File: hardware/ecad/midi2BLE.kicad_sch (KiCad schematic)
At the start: 0 parts

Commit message: Finsihed power schematic, but needs work... pcb has lots of errors still
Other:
- added sheet Battery Sense (battery_sense.kicad_sch)
- added sheet ESP32_S3 (esp32.kicad_sch)
- added sheet OLED UI (oled_ui.kicad_sch)
- added sheet Power (power.kicad_sch)
- added sheet USB Data (usb_data.kicad_sch)
- added sheet VBUS Switching (vbus_switching.kicad_sch)
- note added: "ADC battery monitor"
- note added: "BLE + UI + control"
- note added: "Battery/charging/regulators"
- note added: "Display + status"
- note added: "Keyboard 5V source selection"
- note added: "USB mux/port routing"
- company: (none) -> avega systems
- title: (none) -> midi2BLE_Top_Level

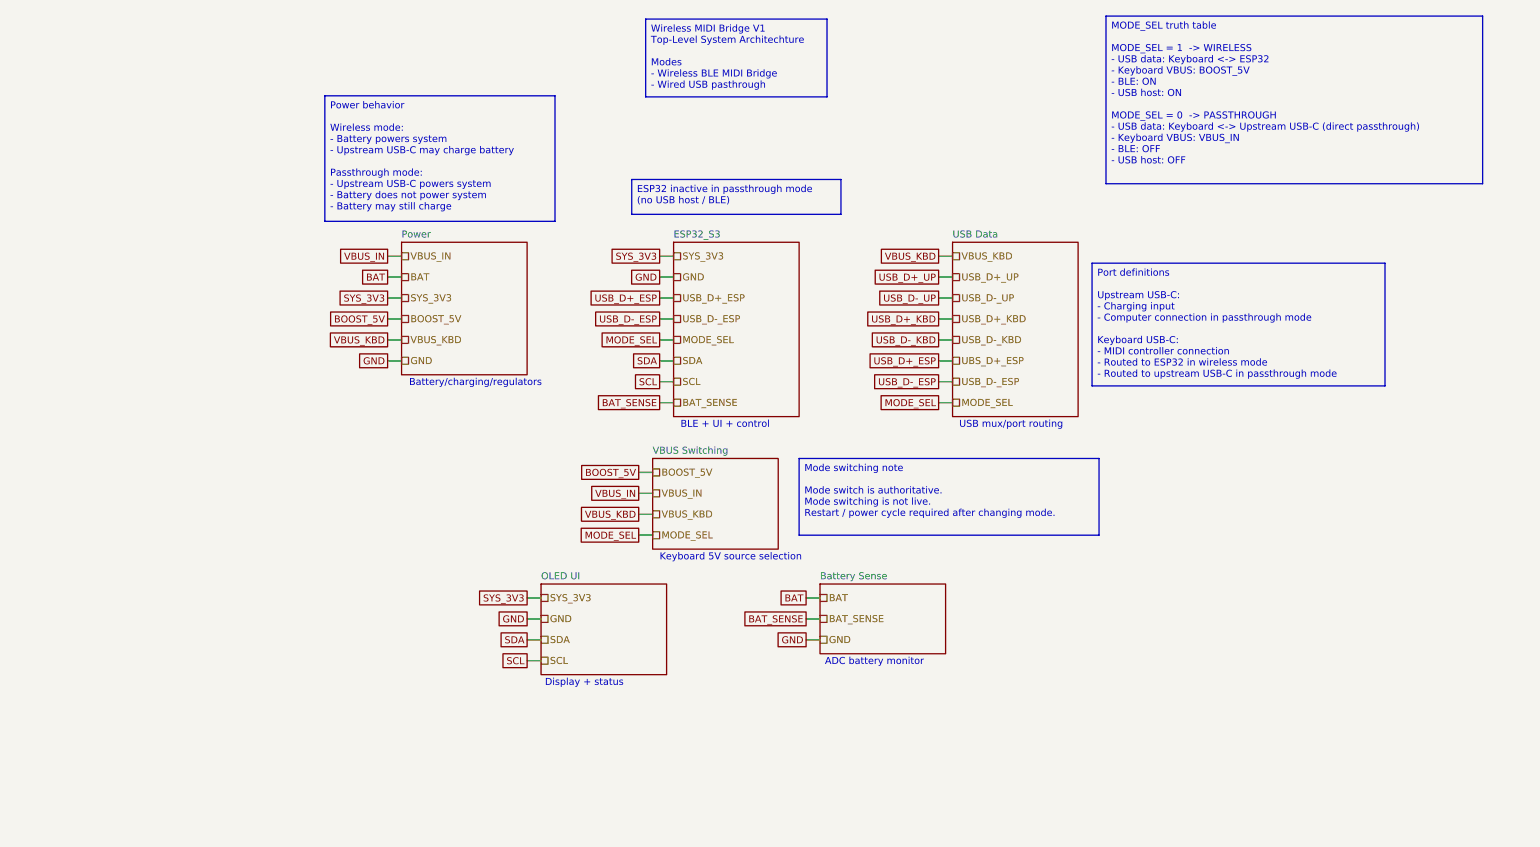
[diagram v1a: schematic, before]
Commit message: Power schematic finished, top level schematic editied to swap from I2c to SPI instead
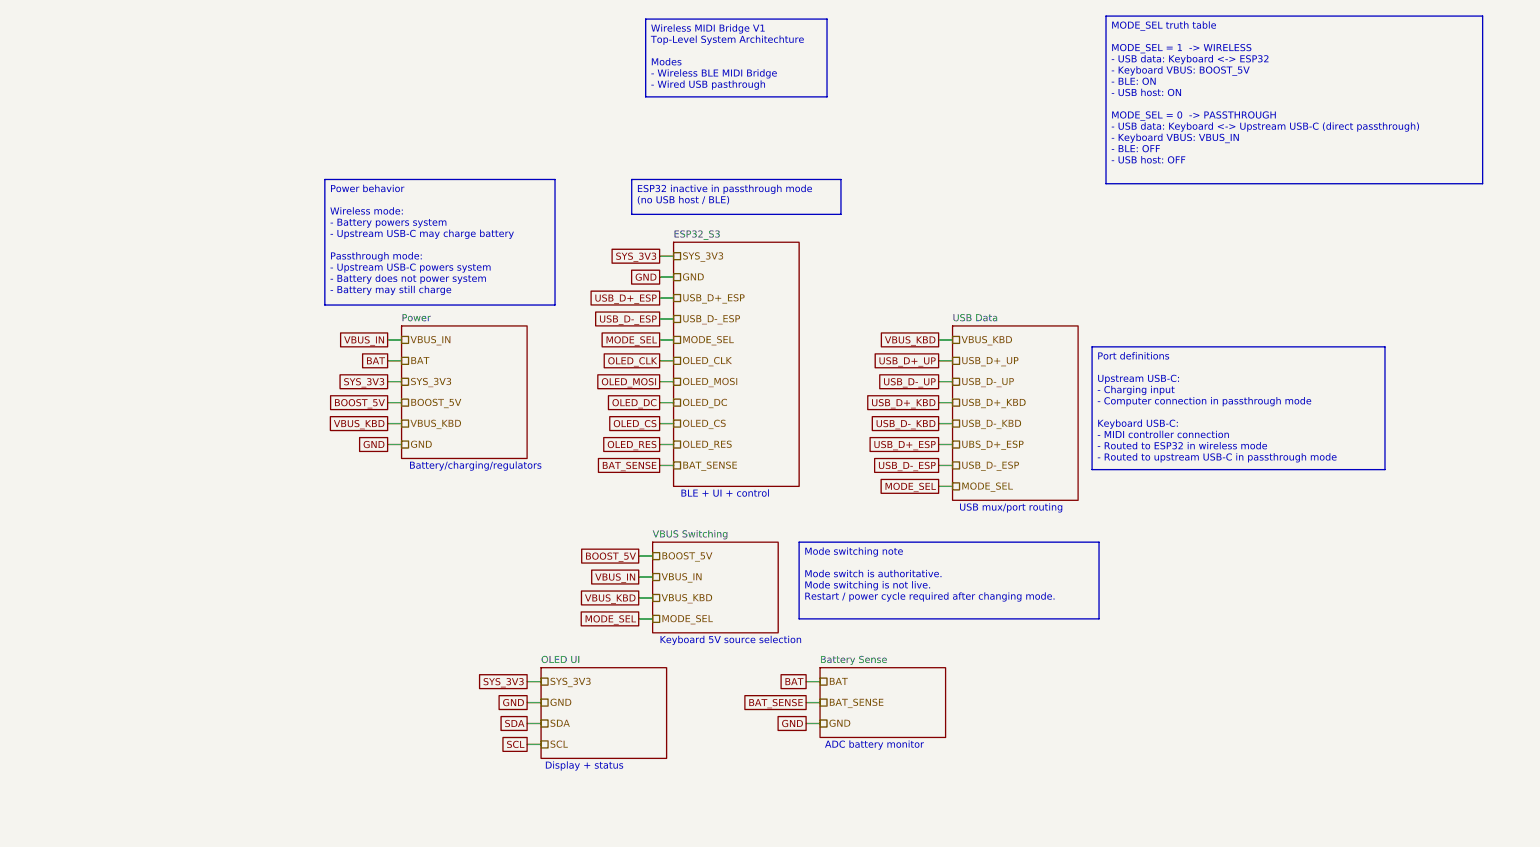
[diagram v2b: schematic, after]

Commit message: finsihed 6/7 sheets, usb_data needs work. Some warnings to be dealt with aswell but no hard errors.
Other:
- sheet Battery Sense ports: added BAT, BAT_SENSE, GND; removed none
- sheet ESP32_S3 ports: added BAT_SENSE, GND, MODE_SEL, OLED_CLK, OLED_CS, OLED_DC, OLED_MOSI, OLED_RES, SYS_3V3, USB_D+_ESP, USB_D-_ESP; removed none
- sheet OLED UI ports: added GND, OLED_CLK, OLED_CS, OLED_DC, OLED_MOSI, OLED_RES, SYS_3V3; removed none
- sheet Power ports: added BAT, BOOST_5V, GND, SYS_3V3, VBUS_IN, VBUS_KBD; removed none
- sheet USB Data ports: added GND, MODE_SEL, SYS_3V3, USB_D+_ESP, USB_D+_KBD, USB_D+_UP, USB_D-_ESP, USB_D-_KBD, USB_D-_UP, VBUS_KBD; removed none
- sheet VBUS Switching ports: added BOOST_5V, GND, MODE_SEL, VBUS_IN, VBUS_KBD; removed none
- company: avega systems -> āvega systems

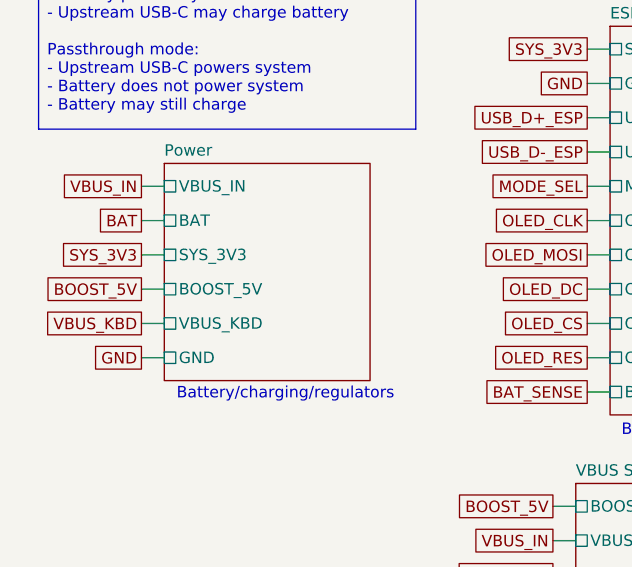
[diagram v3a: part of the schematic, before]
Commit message: Updated schematics to get rid of errors and warnings
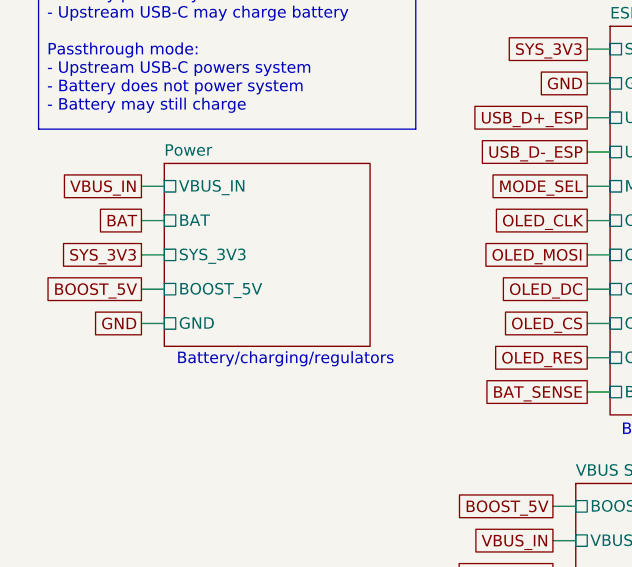
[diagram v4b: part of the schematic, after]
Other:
- sheet Power ports: added none; removed VBUS_KBD
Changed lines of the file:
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@@
 	(text "Battery/charging/regulators"
 		(exclude_from_sim no)
-		(at 98.552 96.774 0)
+		(at 98.552 92.964 0)
 		(effects
 			(font
@@
 	(wire
 		(pts
+			(xy 82.55 88.9) (xy 85.09 88.9)
+		)
+		(stroke
+			(width 0)
+			(type default)
+		)
+	)
+	(wire
+		(pts
 			(xy 132.08 81.28) (xy 134.62 81.28)
 		)
@@
 	(wire
 		(pts
-			(xy 82.55 92.71) (xy 85.09 92.71)
-		)
-		(stroke
-			(width 0)
-			(type default)
-		)
-	)
-	(wire
-		(pts
 			(xy 182.88 92.71) (xy 185.42 92.71)
 		)
@@
 		)
 	)
-	(wire
-		(pts
-			(xy 82.55 88.9) (xy 85.09 88.9)
-		)
-		(stroke
-			(width 0)
-			(type default)
-		)
-	)
 	(global_label "GND"
 		(shape passive)
-		(at 82.55 92.71 180)
-		(fields_autoplaced yes)
-		(effects
-			(font
-				(size 1.27 1.27)
-			)
-			(justify right)
-		)
-		(property "Intersheetrefs" "${INTERSHEET_REFS}"
-			(at 76.8056 92.71 0)
+		(at 82.55 88.9 180)
+		(fields_autoplaced yes)
+		(effects
+			(font
+				(size 1.27 1.27)
+			)
+			(justify right)
+		)
+		(property "Intersheetrefs" "${INTERSHEET_REFS}"
+			(at 76.8056 88.9 0)
 			(hide yes)
 			(show_name no)
@@
 		(property "Intersheetrefs" "${INTERSHEET_REFS}"
 			(at 118.5946 113.03 0)
-			(hide yes)
-			(show_name no)
-			(do_not_autoplace no)
-			(effects
-				(font
-					(size 1.27 1.27)
-				)
-				(justify right)
-			)
-		)
-	)
-	(global_label "VBUS_KBD"
-		(shape passive)
-		(at 82.55 88.9 180)
-		(fields_autoplaced yes)
-		(effects
-			(font
-				(size 1.27 1.27)
-			)
-			(justify right)
-		)
-		(property "Intersheetrefs" "${INTERSHEET_REFS}"
-			(at 70.9999 88.9 0)
 			(hide yes)
 			(show_name no)
@@
 	(sheet
 		(at 85.09 71.12)
-		(size 22.86 24.13)
+		(size 22.86 20.32)
 		(exclude_from_sim no)
 		(in_bom yes)
@@
 		)
 		(property "Sheetfile" "power.kicad_sch"
-			(at 85.09 95.8346 0)
+			(at 85.09 92.0246 0)
 			(hide yes)
 			(show_name no)
@@
 		)
 		(pin "GND" passive
-			(at 85.09 92.71 180)
+			(at 85.09 88.9 180)
 			(effects
 				(font
@@
 			(effects
 				(font
-					(size 1.27 1.27)
-				)
-				(justify left)
-			)
-		)
-		(pin "VBUS_KBD" passive
-			(at 85.09 88.9 180)
-			(effects
-				(font

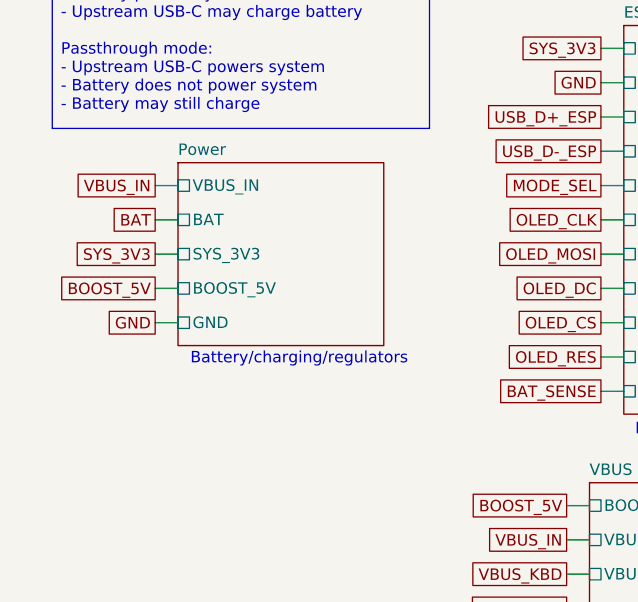
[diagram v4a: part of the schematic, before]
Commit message: feat: complete schematic design for midi2BLE v1
- Add 7-sheet hierarchical schematic covering full system architecture
- Power sheet: BQ24079RGTT charger, TPS62162DSG 3.3V buck, TLV61047DDC
  5V boost, PRTR5V0U2X ESD protection, USB-C receptacle with CC resistors
- ESP32-S3 sheet: WROOM-1-N8R2 module, UART header, boot/reset buttons,
  MODE_SEL debounce circuit, BAT_SENSE ADC input
- OLED UI sheet: SPI SSD1306 connector (GPIO35/36/10/9/8)
- Battery sense sheet: resistor divider for ADC1 battery voltage monitoring
- VBUS switching sheet: TPS2116DRL power mux for BOOST_5V/VBUS_IN selection
- USB data sheet: TS3USB30EDGSR USB 2.0 mux, keyboard USB-B connector,
  PRTR5V0U2X ESD protection on keyboard data lines
- Fix OLED from I2C to SPI, reassign GPIO11/12 away from octal flash
- Fix BQ24079 TS pin from VBUS_IN to 10k resistor to GND
- Set ISET=590R (1.5A charge), ILIM=1k (1.55A input limit) for 2500-3000mAh LiPo
- Pass ERC with 0 errors, 0 warnings (6 ignored: BQ24079 symbol quirks)
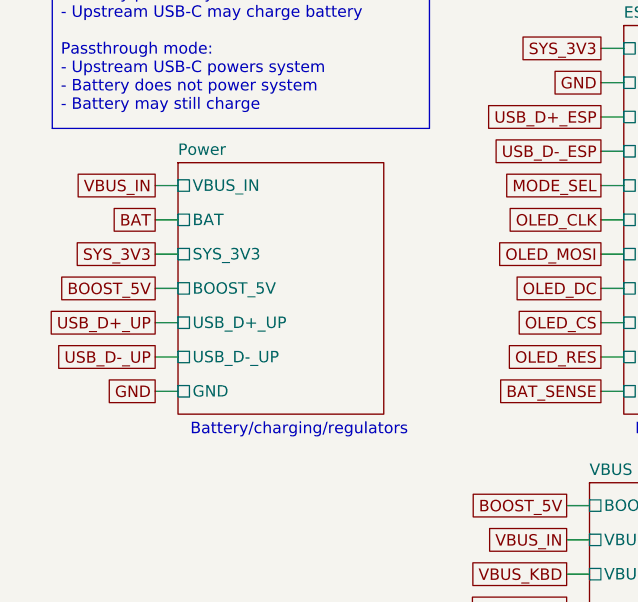
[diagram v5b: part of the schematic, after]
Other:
- sheet Power ports: added USB_D+_UP, USB_D-_UP; removed none

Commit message: docs(hardware): update ecad README to reflect completed schematic and PCB — PCB IS DONE!!!
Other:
- sheet ESP32_S3 ports: added USB_ESP+, USB_ESP-; removed USB_D+_ESP, USB_D-_ESP
- sheet Power ports: added USB_UP+, USB_UP-; removed USB_D+_UP, USB_D-_UP
- sheet USB Data ports: added USB_ESP+, USB_ESP-, USB_KBD+, USB_KBD-, USB_UP+, USB_UP-; removed USB_D+_ESP, USB_D+_KBD, USB_D+_UP, USB_D-_ESP, USB_D-_KBD, USB_D-_UP
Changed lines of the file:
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@@
 		)
 	)
-	(global_label "USB_D-_ESP"
+	(global_label "USB_ESP-"
 		(shape passive)
 		(at 132.08 69.85 180)
@@
 		)
 		(property "Intersheetrefs" "${INTERSHEET_REFS}"
-			(at 117.99 69.85 0)
+			(at 120.2276 69.85 0)
 			(hide yes)
 			(show_name no)
@@
 		)
 	)
-	(global_label "USB_D+_ESP"
+	(global_label "USB_ESP+"
 		(shape passive)
 		(at 132.08 66.04 180)
@@
 		)
 		(property "Intersheetrefs" "${INTERSHEET_REFS}"
-			(at 117.99 66.04 0)
-			(hide yes)
-			(show_name no)
-			(do_not_autoplace no)
-			(effects
-				(font
-					(size 1.27 1.27)
-				)
-				(justify right)
-			)
-		)
-	)
-	(global_label "USB_D+_UP"
+			(at 120.2276 66.04 0)
+			(hide yes)
+			(show_name no)
+			(do_not_autoplace no)
+			(effects
+				(font
+					(size 1.27 1.27)
+				)
+				(justify right)
+			)
+		)
+	)
+	(global_label "USB_UP+"
 		(shape passive)
 		(at 182.88 77.47 180)
@@
 		)
 		(property "Intersheetrefs" "${INTERSHEET_REFS}"
-			(at 169.818 77.47 0)
-			(hide yes)
-			(show_name no)
-			(do_not_autoplace no)
-			(effects
-				(font
-					(size 1.27 1.27)
-				)
-				(justify right)
-			)
-		)
-	)
-	(global_label "USB_D-_UP"
+			(at 172.0556 77.47 0)
+			(hide yes)
+			(show_name no)
+			(do_not_autoplace no)
+			(effects
+				(font
+					(size 1.27 1.27)
+				)
+				(justify right)
+			)
+		)
+	)
+	(global_label "USB_UP-"
 		(shape passive)
 		(at 82.55 92.71 180)
@@
 		)
 		(property "Intersheetrefs" "${INTERSHEET_REFS}"
-			(at 69.488 92.71 0)
-			(hide yes)
-			(show_name no)
-			(do_not_autoplace no)
-			(effects
-				(font
-					(size 1.27 1.27)
-				)
-				(justify right)
-			)
-		)
-	)
-	(global_label "USB_D-_UP"
+			(at 71.7256 92.71 0)
+			(hide yes)
+			(show_name no)
+			(do_not_autoplace no)
+			(effects
+				(font
+					(size 1.27 1.27)
+				)
+				(justify right)
+			)
+		)
+	)
+	(global_label "USB_UP-"
 		(shape passive)
 		(at 182.88 81.28 180)
@@
 		)
 		(property "Intersheetrefs" "${INTERSHEET_REFS}"
-			(at 169.818 81.28 0)
+			(at 172.0556 81.28 0)
 			(hide yes)
 			(show_name no)
@@
 		)
 	)
-	(global_label "USB_D-_ESP"
+	(global_label "USB_ESP-"
 		(shape passive)
 		(at 182.88 96.52 180)
@@
 		)
 		(property "Intersheetrefs" "${INTERSHEET_REFS}"
-			(at 168.79 96.52 0)
-			(hide yes)
-			(show_name no)
-			(do_not_autoplace no)
-			(effects
-				(font
-					(size 1.27 1.27)
-				)
-				(justify right)
-			)
-		)
-	)
-	(global_label "USB_D-_KBD"
+			(at 171.0276 96.52 0)
+			(hide yes)
+			(show_name no)
+			(do_not_autoplace no)
+			(effects
+				(font
+					(size 1.27 1.27)
+				)
+				(justify right)
+			)
+		)
+	)
+	(global_label "USB_KBD-"
 		(shape passive)
 		(at 182.88 88.9 180)
@@
 		)
 		(property "Intersheetrefs" "${INTERSHEET_REFS}"
-			(at 168.6085 88.9 0)
+			(at 170.8461 88.9 0)
 			(hide yes)
 			(show_name no)
@@
 		)
 	)
-	(global_label "USB_D+_UP"
+	(global_label "USB_UP+"
 		(shape passive)
 		(at 82.55 88.9 180)
@@
 		)
 		(property "Intersheetrefs" "${INTERSHEET_REFS}"
-			(at 69.488 88.9 0)
-			(hide yes)
-			(show_name no)
-			(do_not_autoplace no)
-			(effects
-				(font
-					(size 1.27 1.27)
-				)
-				(justify right)
-			)
-		)
-	)
-	(global_label "USB_D+_KBD"
+			(at 71.7256 88.9 0)
+			(hide yes)
+			(show_name no)
+			(do_not_autoplace no)
+			(effects
+				(font
+					(size 1.27 1.27)
+				)
+				(justify right)
+			)
+		)
+	)
+	(global_label "USB_KBD+"
 		(shape passive)
 		(at 182.88 85.09 180)
@@
 		)
 		(property "Intersheetrefs" "${INTERSHEET_REFS}"
-			(at 168.6085 85.09 0)
+			(at 170.8461 85.09 0)
 			(hide yes)
 			(show_name no)
@@
 		)
 	)
-	(global_label "USB_D+_ESP"
+	(global_label "USB_ESP+"
 		(shape passive)
 		(at 182.88 92.71 180)
@@
 		)
 		(property "Intersheetrefs" "${INTERSHEET_REFS}"
-			(at 168.79 92.71 0)
+			(at 171.0276 92.71 0)
 			(hide yes)
 			(show_name no)
@@
 			)
 		)
-		(pin "USB_D+_ESP" passive
+		(pin "USB_ESP+" passive
 			(at 185.42 92.71 180)
 			(effects
@@
 			)
 		)
-		(pin "USB_D+_KBD" passive
+		(pin "USB_KBD+" passive
 			(at 185.42 85.09 180)
 			(effects
@@
 			)
 		)
-		(pin "USB_D+_UP" passive
+		(pin "USB_UP+" passive
 			(at 185.42 77.47 180)
 			(effects
@@
 			)
 		)
-		(pin "USB_D-_ESP" passive
+		(pin "USB_ESP-" passive
 			(at 185.42 96.52 180)
 			(effects
@@
 			)
 		)
-		(pin "USB_D-_KBD" passive
+		(pin "USB_KBD-" passive
 			(at 185.42 88.9 180)
 			(effects
@@
 			)
 		)
-		(pin "USB_D-_UP" passive
+		(pin "USB_UP-" passive
 			(at 185.42 81.28 180)
 			(effects
@@
 			)
 		)
-		(pin "USB_D+_UP" passive
+		(pin "USB_UP+" passive
 			(at 85.09 88.9 180)
 			(effects
@@
 			)
 		)
-		(pin "USB_D-_UP" passive
+		(pin "USB_UP-" passive
 			(at 85.09 92.71 180)
 			(effects
@@
 			)
 		)
-		(pin "USB_D+_ESP" passive
+		(pin "USB_ESP+" passive
 			(at 134.62 66.04 180)
 			(effects
@@
 			)
 		)
-		(pin "USB_D-_ESP" passive
+		(pin "USB_ESP-" passive
 			(at 134.62 69.85 180)
 			(effects
